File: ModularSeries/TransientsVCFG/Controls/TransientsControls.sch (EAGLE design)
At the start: 25 parts, among them SW1 PVA1_DPST, SW2 PVA2_DPDT, SW3 PVA1_DPST, SW4 PVA2_DPDT

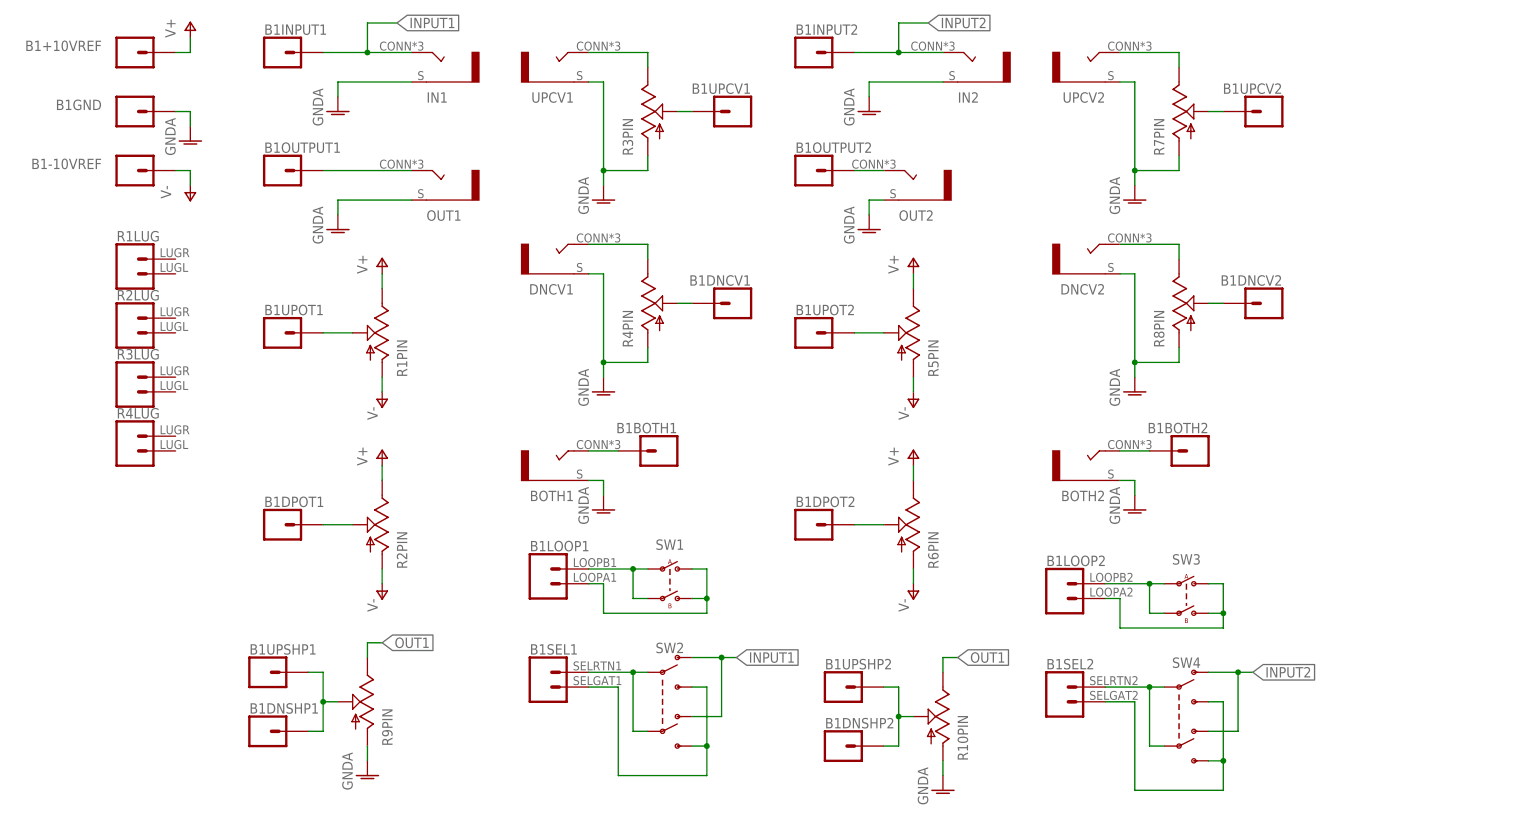
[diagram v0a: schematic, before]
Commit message: Folder cleaned up, Transients added
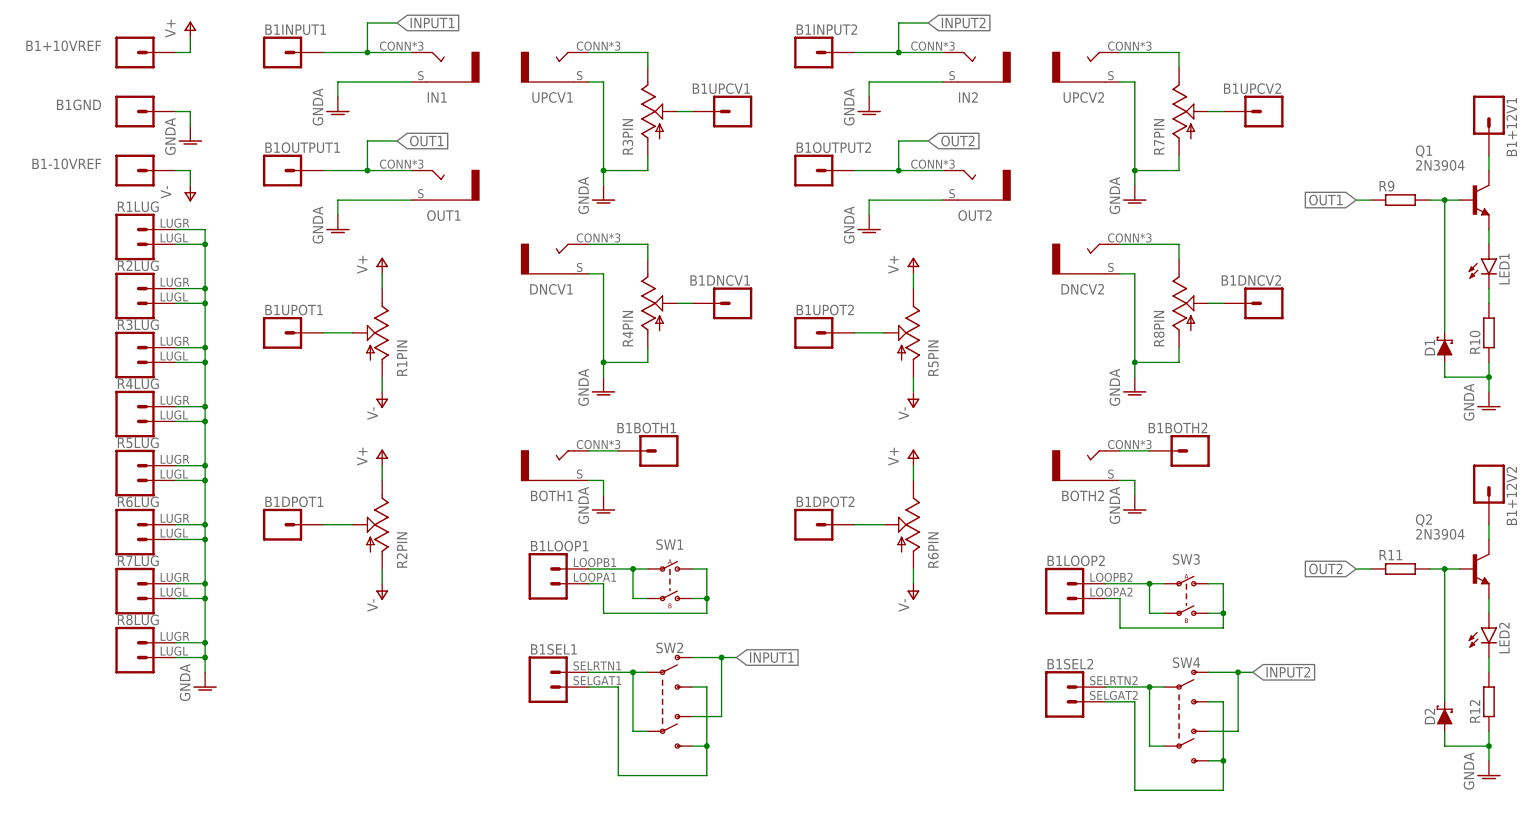
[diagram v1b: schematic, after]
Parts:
- added D1, D2: (no value), ElectricNoodleBox:SCHOTTKY_DO35
- added LED1, LED2: (no value), led:LED5MM
- added Q1, Q2: 2N3904, transistor-neu-to92:2N3904
- added R11, R12: (no value), rcl:R-EU_0207/10
- R10, R9: device ElectricNoodleBox:POTENTIOMETER -> rcl:R-EU_0207/10
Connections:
- removed net N$9: B1OUTPUT2.1, OUT2.T
- new net N$27: LED1.C, R10.2
- new net N$28: D2.C, Q2.B, R11.2
- new net N$29: LED2.A, Q2.E
- new net N$30: LED2.C, R12.2
- new net N$31: B1+12V2.1, Q2.C
- new net OUT2: B1OUTPUT2.1, OUT2.T, R11.1
- net GNDA: now also D1.A, D2.A, R10.1, R12.1, R1LUG.1, R1LUG.2, R2LUG.1, R2LUG.2, R3LUG.1, R3LUG.2, R4LUG.1, R4LUG.2, R5LUG.1, R5LUG.2, R6LUG.1, R6LUG.2, R7LUG.1, R7LUG.2, R8LUG.1, R8LUG.2; no longer R10PIN.A, R9PIN.A
- net N$1: now also B1+12V1.1, Q1.C; no longer B1OUTPUT1.1, OUT1.T
- net N$25: now also D1.C, Q1.B, R9.2; no longer B1DNSHP1.1, B1UPSHP1.1, R9PIN.W
- net N$26: now also LED1.A, Q1.E; no longer B1DNSHP2.1, B1UPSHP2.1, R10PIN.W
- net OUT1: now also B1OUTPUT1.1, OUT1.T, R9.1; no longer R10PIN.B, R9PIN.B
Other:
- moved on the sheet: OUT2, R1LUG, R2LUG, R3LUG, R4LUG

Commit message: All active BOMs updated to new header standard
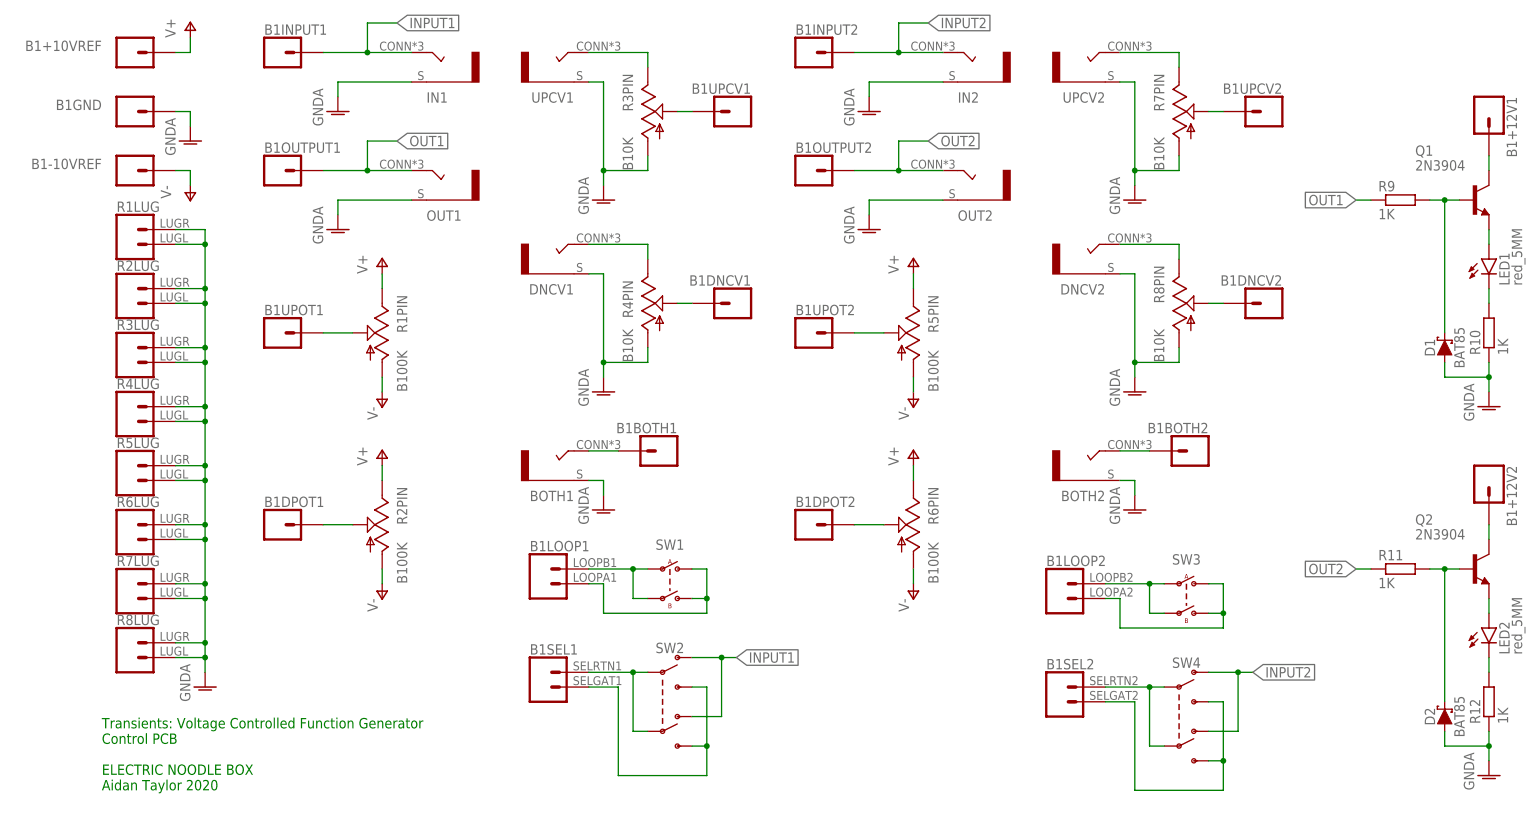
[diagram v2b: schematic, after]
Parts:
- D1, D2: value (none) -> BAT85
- LED1, LED2: value (none) -> red_5MM
- R1, R2, R5, R6: value (none) -> B100K
- R10, R11, R12, R9: value (none) -> 1K
- R3, R4, R7, R8: value (none) -> B10K
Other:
- note added: "Transients: Voltage Controlled Function Generator Control PCB ELECTRIC NOODLE BOX Aidan Taylor 2020"
